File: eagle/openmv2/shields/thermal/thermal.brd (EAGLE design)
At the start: 35.6 x 26.7 mm, 10 parts, among them U1 MLX90620, U3 2.6v

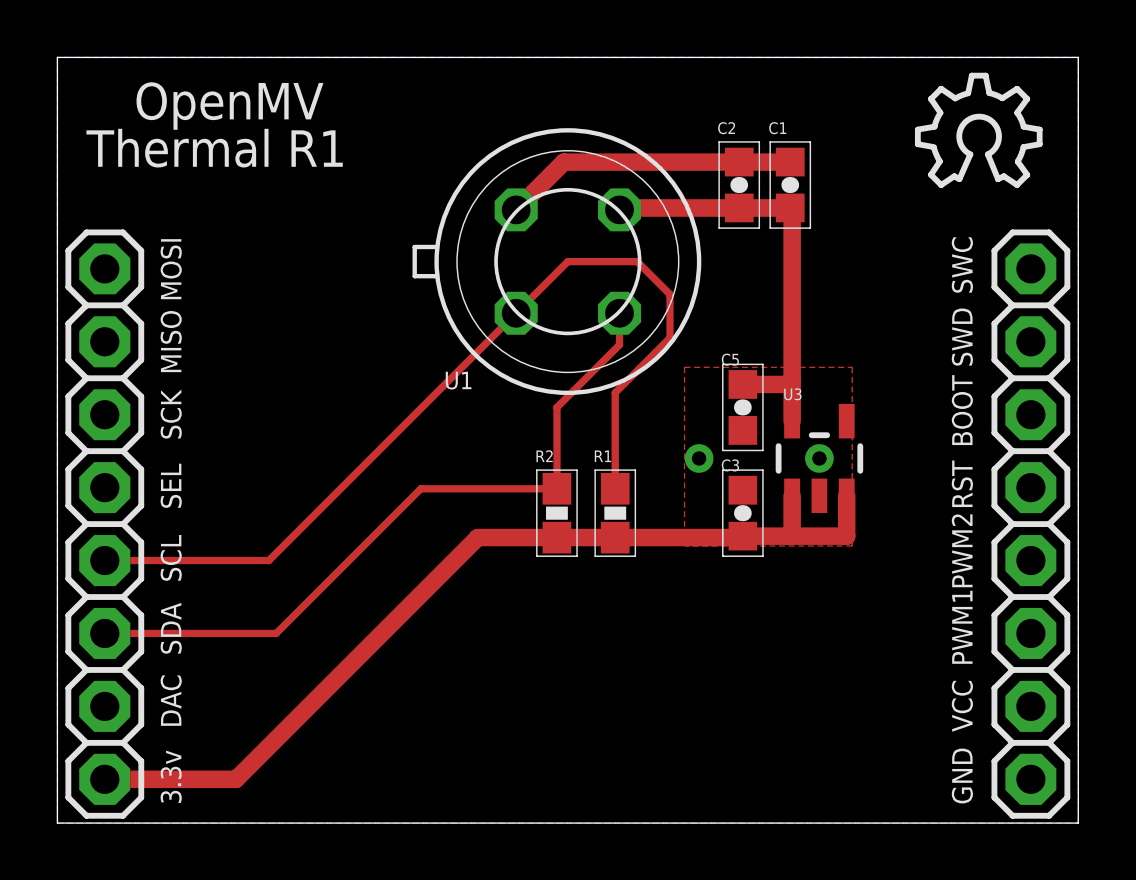
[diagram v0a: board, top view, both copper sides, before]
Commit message: Update shields silk-screen.
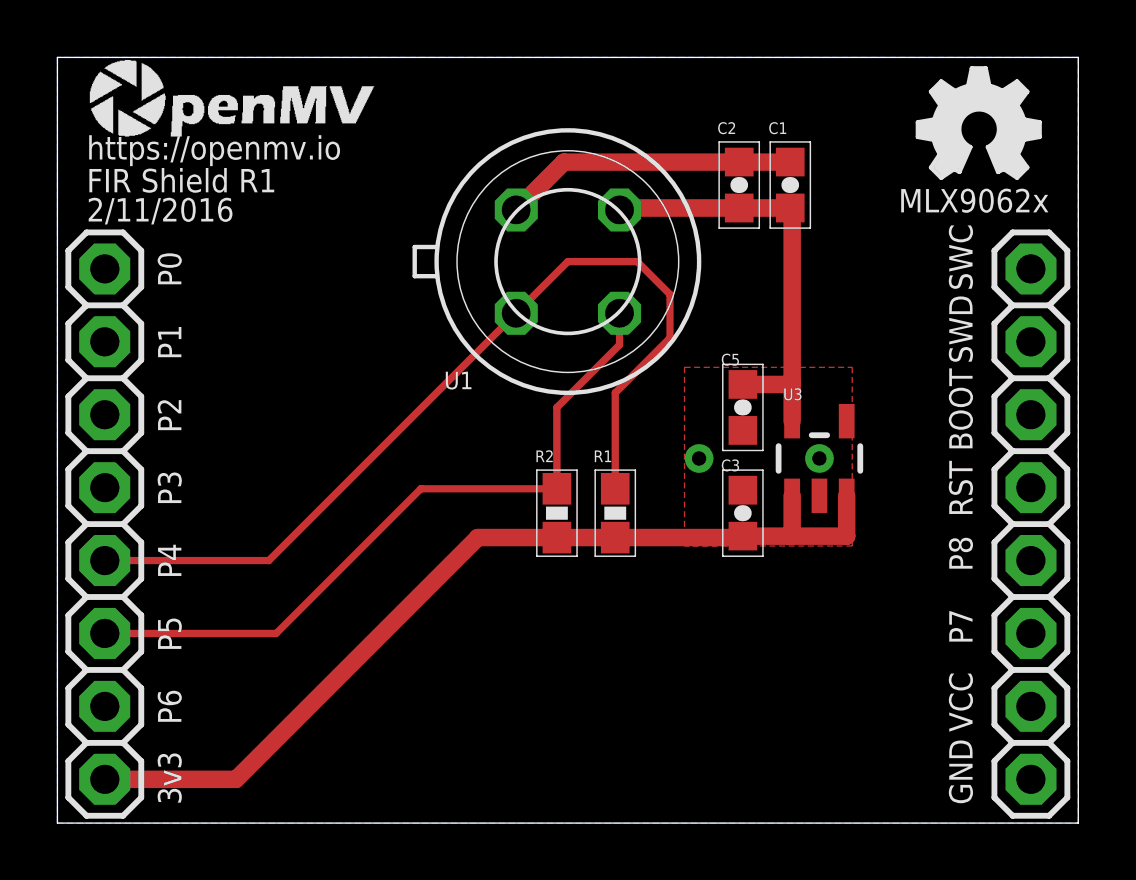
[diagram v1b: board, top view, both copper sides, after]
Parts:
- removed LOGO1: OSHW_LOGO_8MILX0150-NT, iofault:OSHW_8X150_NOTEXT
- added U$10: (no value), openmv:OMV-LOGO-SMALL
- added U$3: (no value), openmv:OMV-LOGO
- added U$5: (no value), openmv:ROHS
- added U$6: (no value), openmv:WEEE
- added U$7: (no value), iofault:OSHW_FILLX150_NOTEXT
- U1: value MLX90620 -> MLX9062x
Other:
- board text added: "2/11/2016"
- board text added: "3v3"
- board text added: "Built by MacroFab"
- board text added: "FIR Shield R1"
- board text added: "MLX9062x"
- board text added: "Made in USA"
- board text added: "P0"
- board text added: "P1"
- board text added: "P2"
- board text added: "P3"
- board text added: "P4"
- board text added: "P5"
- board text added: "P6"
- board text added: "P7"
- board text added: "P8"
- board text added: "https://openmv.io"
- board text removed: "0.5 oz copper"
- board text removed: "1 oz copper"
- board text removed: "3.3v"
- board text removed: "47 mil core"
- board text removed: "6.7 mil prepreg"
- board text removed: "Antenna trace 12mils (50Ohms impedance)"
- board text removed: "DAC"
- board text removed: "MISO"
- board text removed: "MOSI"
- board text removed: "OpenMV"
- board text removed: "PWM1"
- board text removed: "PWM2"
- board text removed: "SCK"
- board text removed: "SCL"
- board text removed: "SDA"
- board text removed: "SEL"
- board text removed: "Stackup:"
- board text removed: "Thermal R1"
- board text removed: "er is 3.66"
